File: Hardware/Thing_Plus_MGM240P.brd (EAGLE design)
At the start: 22.9 x 58.4 mm, 181 parts, among them J1 THING_PLUS_LOGICAL, J2 USB Female Type C Connector, J3 QWIIC_RIGHT_ANGLE, J5 MICRO-SDFRICTION, Q1 20V/4.2A/52mΩ/1.4W, U1 MGM240P, U2 XC6222B331MR-G, U3 EFM32GG12B410F1024GL120, U4 MCP73831, U5 MAX17048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

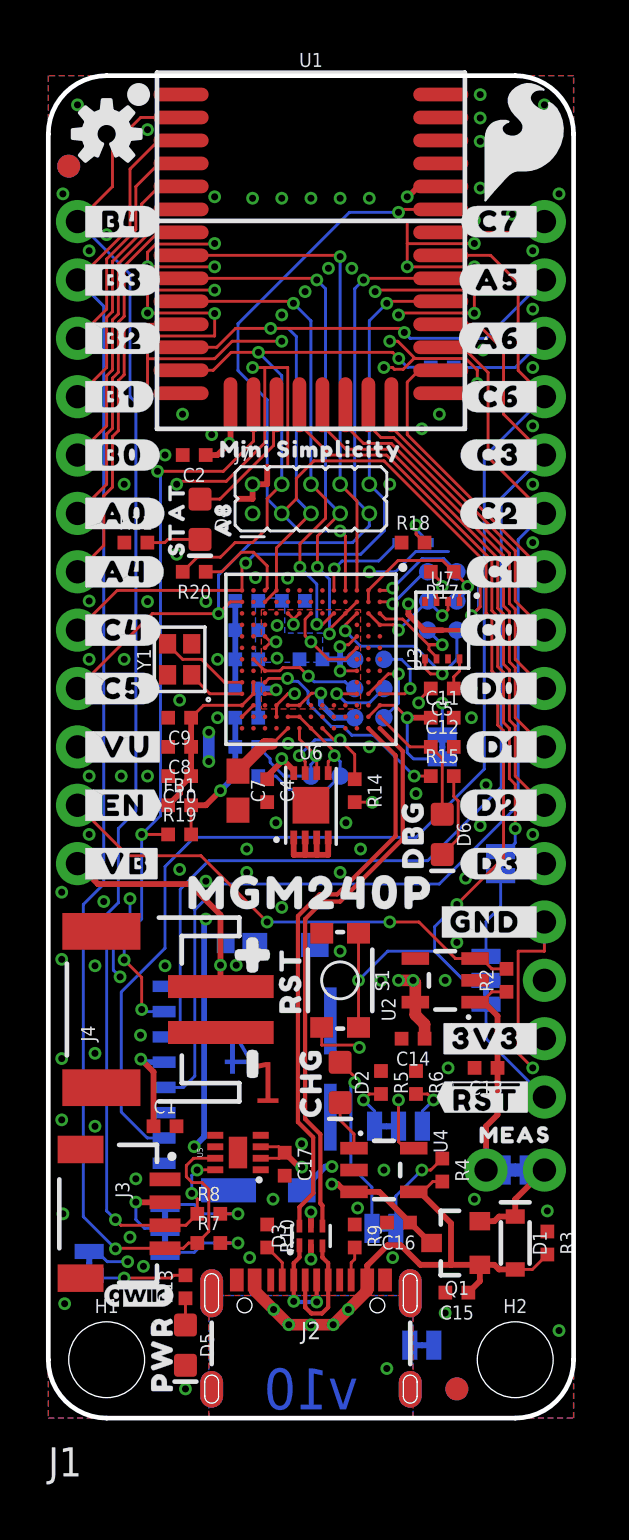
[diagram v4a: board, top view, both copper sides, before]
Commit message: Design review updates
Move RST jumper to align with D3_ISO jumper
Add silk label to CHG_I jumper
Move R20 left 25 mils
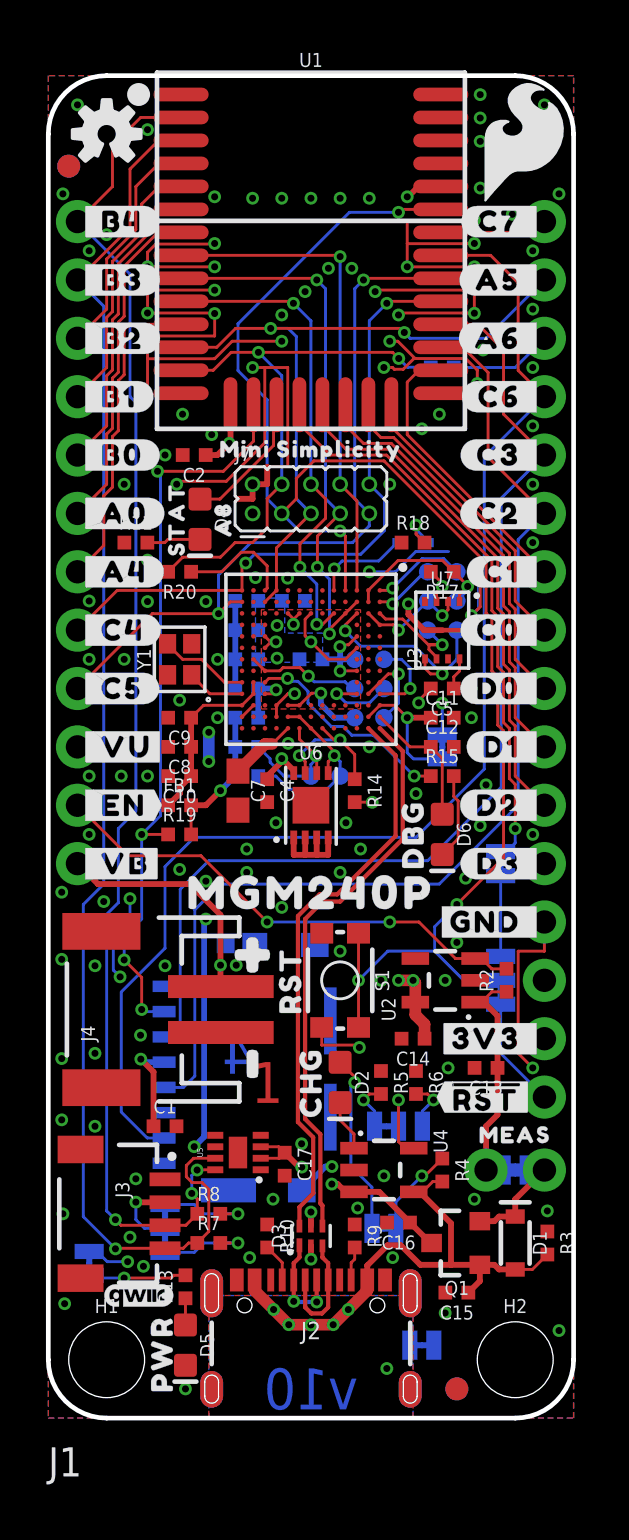
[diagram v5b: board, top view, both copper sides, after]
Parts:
- added U$83: (no value), output:#CHG_I#0
- moved U$80 0.64 mm to (19.1, 18.2)
- moved U$81 0.64 mm to (19.1, 19.9)
- moved R20 0.63 mm to (5.71, 36.8)
- moved RST 0.63 mm to (19.7, 19.1)
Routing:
- net RX/PA06: track 24.3 -> 24.9 mm
- net !RESET!: track 66.8 -> 67.5 mm
- net N$25: track 4.38 -> 5.01 mm
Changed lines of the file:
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@@
 <attribute name="VALUE" x="5.715" y="24.838" size="0.6096" layer="27" font="vector" ratio="20" align="top-center"/>
 </element>
-<element name="R20" library="SparkFun-Resistors" package="0402-TIGHT" value="330" x="6.35" y="36.83" smashed="yes" rot="R180">
-<attribute name="NAME" x="6.35" y="36.268" size="0.6096" layer="25" font="vector" ratio="20" rot="R180" align="bottom-center"/>
-<attribute name="PROD_ID" value="RES-15407" x="6.35" y="36.83" size="1.778" layer="27" rot="R180" display="off"/>
-<attribute name="VALUE" x="6.35" y="37.392" size="0.6096" layer="27" font="vector" ratio="20" rot="R180" align="top-center"/>
+<element name="R20" library="SparkFun-Resistors" package="0402-TIGHT" value="330" x="5.715" y="36.83" smashed="yes" rot="R180">
+<attribute name="NAME" x="5.715" y="36.268" size="0.6096" layer="25" font="vector" ratio="20" rot="R180" align="bottom-center"/>
+<attribute name="PROD_ID" value="RES-15407" x="5.715" y="36.83" size="1.778" layer="27" rot="R180" display="off"/>
+<attribute name="VALUE" x="5.715" y="37.392" size="0.6096" layer="27" font="vector" ratio="20" rot="R180" align="top-center"/>
 </element>
 <element name="R21" library="SparkFun-Resistors" package="0402-TIGHT" value="330" x="17.145" y="45.72" smashed="yes" rot="MR0">
@@
 </element>
 <element name="U$65" library="SEGGER-LOGO" package="SEGGER_LOGO" value="" x="9.269" y="44.45" smashed="yes" rot="MR0"/>
-<element name="RST" library="SparkFun-Jumpers" package="SMT-JUMPER_3_1-NC_TRACE_SILK" package3d_urn="urn:adsk.eagle:package:39288/1" value="JUMPER-SMT_3_1-NC_TRACE_SILK" x="19.05" y="19.05" smashed="yes" rot="MR270">
-<attribute name="NAME" x="17.907" y="19.05" size="0.6096" layer="26" font="vector" ratio="20" rot="MR270" align="bottom-center"/>
-<attribute name="VALUE" x="20.193" y="19.05" size="0.6096" layer="28" font="vector" ratio="20" rot="MR270" align="top-center"/>
+<element name="RST" library="SparkFun-Jumpers" package="SMT-JUMPER_3_1-NC_TRACE_SILK" package3d_urn="urn:adsk.eagle:package:39288/1" value="JUMPER-SMT_3_1-NC_TRACE_SILK" x="19.685" y="19.05" smashed="yes" rot="MR270">
+<attribute name="NAME" x="18.542" y="19.05" size="0.6096" layer="26" font="vector" ratio="20" rot="MR270" align="bottom-center"/>
+<attribute name="VALUE" x="20.828" y="19.05" size="0.6096" layer="28" font="vector" ratio="20" rot="MR270" align="top-center"/>
 </element>
 <element name="D3_ISO" library="SparkFun-Jumpers" package="SMT-JUMPER_2_NC_TRACE_SILK" package3d_urn="urn:adsk.eagle:package:39281/1" value="JUMPER-SMT_2_NC_TRACE_SILK" x="19.685" y="24.13" smashed="yes" rot="MR270">
@@
 <attribute name="VALUE" x="20.828" y="24.13" size="0.6096" layer="28" font="vector" ratio="20" rot="MR270" align="top-center"/>
 </element>
-<element name="U$80" library="output" package="#RST#0" value="" x="18.415" y="18.161" smashed="yes" rot="MR0"/>
-<element name="U$81" library="output" package="#D3#0" value="" x="18.415" y="19.939" smashed="yes" rot="MR0"/>
+<element name="U$80" library="output" package="#RST#0" value="" x="19.05" y="18.161" smashed="yes" rot="MR0"/>
+<element name="U$81" library="output" package="#D3#0" value="" x="19.05" y="19.939" smashed="yes" rot="MR0"/>
 <element name="U$82" library="output" package="#D3#4" value="" x="16.383" y="22.1615" smashed="yes" rot="MR0"/>
 <element name="U$47" library="SILICON-LABS-LOGO" package="SILICON_LABS_LOGO" value="" x="6.096" y="56.007" smashed="yes" rot="MR0"/>
+<element name="U$83" library="output" package="#CHG_I#0" value="" x="15.24" y="11.176" smashed="yes" rot="MR0"/>
 </elements>
 <signals>
@@
 <via x="17.272" y="19.05" extent="1-16" drill="0.3048"/>
 <via x="17.399" y="15.24" extent="1-16" drill="0.3048"/>
-<via x="14.605" y="10.795" extent="1-16" drill="0.3048"/>
+<via x="14.605" y="10.541" extent="1-16" drill="0.3048"/>
 <wire x1="18.5337" y1="48.0905" x2="18.542" y2="48.0822" width="0.127" layer="1"/>
 <wire x1="18.5337" y1="48.0905" x2="15.3245" y2="48.0905" width="0.127" layer="1"/>
@@
 <wire x1="11.4308875" y1="7.4939125" x2="11.4308875" y2="6.9164" width="0.254" layer="1"/>
 <via x="11.4308875" y="6.9164" extent="1-16" drill="0.3048"/>
-<via x="5.588" y="37.592" extent="1-16" drill="0.3048"/>
+<via x="4.318" y="37.338" extent="1-16" drill="0.3048"/>
 <via x="19.05" y="27.559" extent="1-16" drill="0.3048"/>
 <via x="18.796" y="25.781" extent="1-16" drill="0.3048"/>
@@
 <contactref element="R4" pad="1"/>
 <contactref element="CHG" pad="1"/>
-<via x="16.256" y="10.795" extent="1-16" drill="0.3048"/>
-<wire x1="16.256" y1="10.795" x2="16.645" y2="10.795" width="0.127" layer="1"/>
-<wire x1="16.645" y1="10.795" x2="17.145" y2="11.295" width="0.127" layer="1"/>
-<wire x1="15.1257" y1="8.255" x2="15.1257" y2="9.6647" width="0.127" layer="16"/>
-<wire x1="15.1257" y1="9.6647" x2="16.256" y2="10.795" width="0.127" layer="16"/>
+<via x="16.256" y="10.541" extent="1-16" drill="0.3048"/>
+<wire x1="16.256" y1="10.541" x2="16.391" y2="10.541" width="0.127" layer="1"/>
+<wire x1="16.391" y1="10.541" x2="17.145" y2="11.295" width="0.127" layer="1"/>
+<wire x1="15.1257" y1="8.255" x2="15.1257" y2="9.4107" width="0.127" layer="16"/>
+<wire x1="15.1257" y1="9.4107" x2="16.256" y2="10.541" width="0.127" layer="16"/>
 </signal>
 <signal name="N$14">
@@
 <wire x1="9.525" y1="40.005" x2="10.16" y2="40.64" width="0.127" layer="1"/>
 <contactref element="R20" pad="2"/>
-<wire x1="5.85" y1="36.83" x2="6.485" y2="37.465" width="0.127" layer="1"/>
+<wire x1="5.215" y1="36.83" x2="5.85" y2="37.465" width="0.127" layer="1"/>
 <wire x1="7.493" y1="37.465" x2="8.128" y2="38.1" width="0.127" layer="1"/>
-<wire x1="6.485" y1="37.465" x2="7.493" y2="37.465" width="0.127" layer="1"/>
+<wire x1="5.85" y1="37.465" x2="7.493" y2="37.465" width="0.127" layer="1"/>
 <wire x1="8.128" y1="38.1" x2="8.89" y2="38.1" width="0.127" layer="1"/>
 <wire x1="8.89" y1="38.1" x2="9.525" y2="38.735" width="0.127" layer="1"/>
@@
 <via x="13.5" y="19.05" extent="1-16" drill="0.3048"/>
 <wire x1="13.5" y1="19.05" x2="14.77" y2="20.32" width="0.127" layer="16"/>
-<wire x1="18.0815" y1="19.05" x2="19.05" y2="19.05" width="0.127" layer="16"/>
+<wire x1="18.0815" y1="19.05" x2="19.685" y2="19.05" width="0.127" layer="16"/>
 <wire x1="16.8115" y1="20.32" x2="18.0815" y2="19.05" width="0.127" layer="16"/>
 <wire x1="14.77" y1="20.32" x2="16.8115" y2="20.32" width="0.127" layer="16"/>
@@
 <wire x1="9.525" y1="37.084" x2="8.9281" y2="37.6809" width="0.127" layer="1"/>
 <wire x1="8.39645625" y1="37.6809" x2="8.9281" y2="37.6809" width="0.127" layer="1"/>
-<wire x1="6.85" y1="36.83" x2="7.54555625" y2="36.83" width="0.127" layer="1"/>
+<wire x1="6.215" y1="36.83" x2="7.54555625" y2="36.83" width="0.127" layer="1"/>
 <wire x1="7.54555625" y1="36.83" x2="8.39645625" y2="37.6809" width="0.127" layer="1"/>
 </signal>
@@
 <contactref element="RST" pad="3"/>
 <contactref element="J1" pad="28"/>
-<wire x1="21.59" y1="13.97" x2="19.05" y2="16.51" width="0.127" layer="16"/>
-<wire x1="19.05" y1="16.51" x2="19.05" y2="18.0086" width="0.127" layer="16"/>
+<wire x1="21.59" y1="13.97" x2="19.685" y2="15.875" width="0.127" layer="16"/>
+<wire x1="19.685" y1="15.875" x2="19.685" y2="18.0086" width="0.127" layer="16"/>
 </signal>
 <signal name="A0">
@@
 <contactref element="D3_ISO" pad="2"/>
 <contactref element="J1" pad="24"/>
-<wire x1="19.685" y1="23.6093" x2="19.685" y2="22.2504" width="0.127" layer="16"/>
-<wire x1="19.685" y1="22.2504" x2="19.05" y2="21.6154" width="0.127" layer="16"/>
-<wire x1="19.05" y1="21.6154" x2="19.05" y2="20.0914" width="0.127" layer="16"/>
+<wire x1="19.685" y1="23.6093" x2="19.685" y2="20.0914" width="0.127" layer="16"/>
 <wire x1="19.685" y1="23.6093" x2="21.0693" y2="23.6093" width="0.127" layer="16"/>
 <wire x1="21.0693" y1="23.6093" x2="21.59" y2="24.13" width="0.127" layer="16"/>

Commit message: Design review updates
Nudge RX/PA06 away from N$25
Add text to schematic explaining escape routing connections
Change RST jumper to "JP1" to make people read the docs
Remove "Thing Plus" from bottom silkscreen
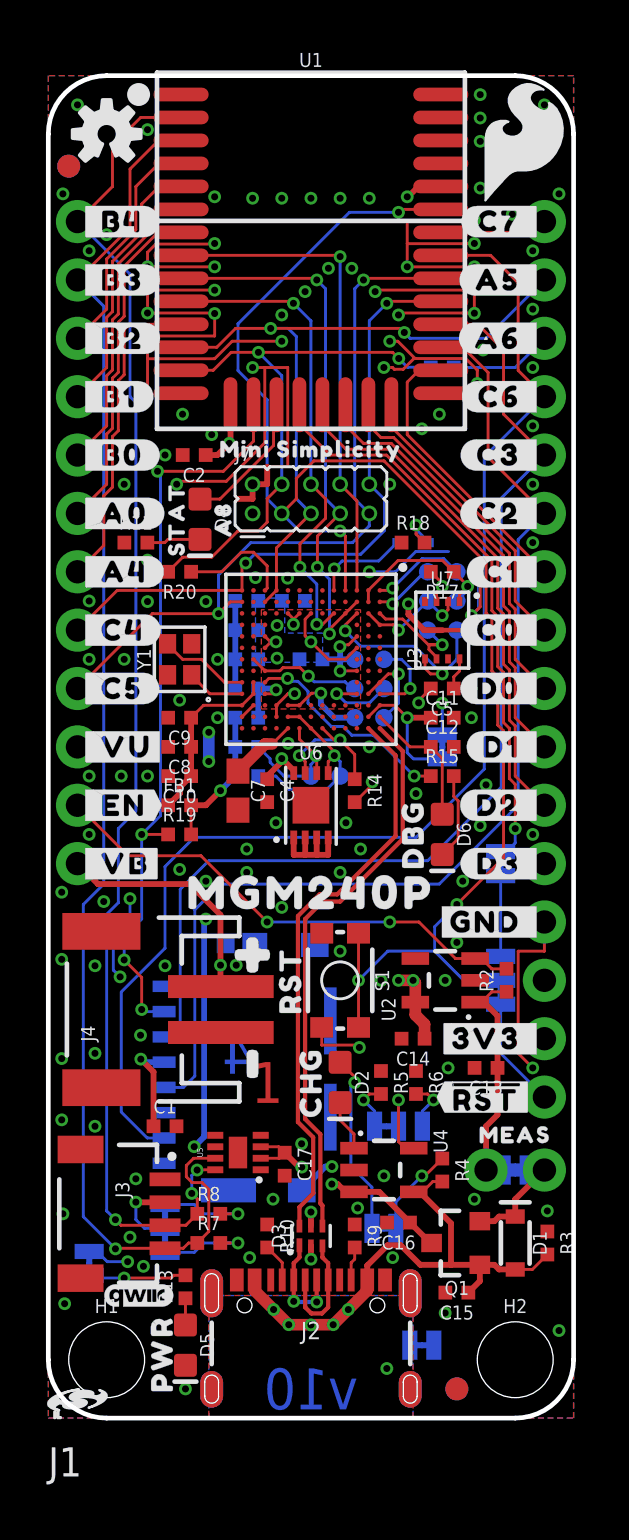
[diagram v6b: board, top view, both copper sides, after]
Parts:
- removed U$80: (no value), output:#RST#0
- removed U$81: (no value), output:#D3#0
- U$69: device output:THING_PLUS0 -> output:#JP1#0
- moved U$69 10.6 mm to (19.1, 18.2)
- moved U$82 3.21 mm to (18.9, 24.1)
- moved U$58 2.74 mm to (11.4, 26.7)
- renumbered RST to JP1

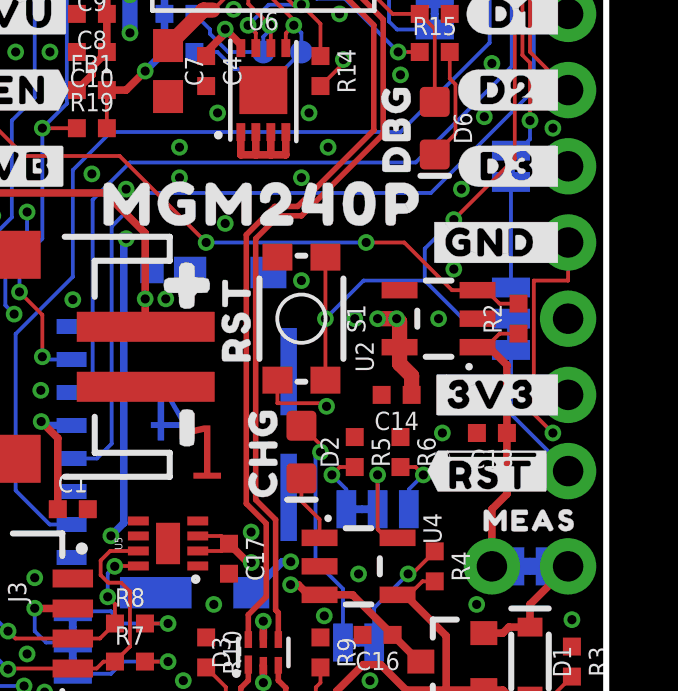
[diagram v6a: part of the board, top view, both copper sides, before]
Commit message: Design review changes
Fix acid traps
Change JP1 silk
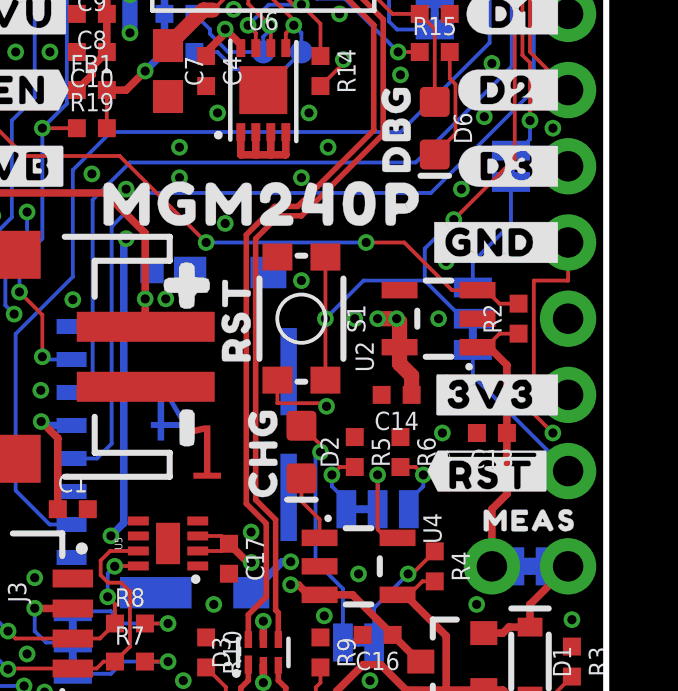
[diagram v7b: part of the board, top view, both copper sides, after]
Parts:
- added U$80: (no value), output:A0
- added U$81: (no value), output:B0
- moved JP1 1.27 mm to (18.4, 19.1)
- moved U$69 1.26 mm to (19.9, 19.1), turned to 90 degrees
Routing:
- net !RESET!: track 67.5 -> 66.2 mm
- net N$28: track 4.83 -> 5.35 mm
- net A0: track 5.64 -> 6.16 mm
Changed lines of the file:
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@@
 <vertex x="0.408365625" y="0.00025625"/>
 </polygon>
-<wire x1="15.875" y1="24.13" x2="15.24" y2="24.13" width="0.1524" layer="22"/>
-<wire x1="15.367" y1="19.558" x2="18.669" y2="19.558" width="0.1524" layer="22"/>
-<wire x1="15.24" y1="24.13" x2="14.605" y2="23.495" width="0.1524" layer="22"/>
-<wire x1="14.605" y1="23.495" x2="14.605" y2="20.32" width="0.1524" layer="22"/>
-<wire x1="14.605" y1="20.32" x2="15.367" y2="19.558" width="0.1524" layer="22"/>
 </plain>
 <attributes>
@@
 </element>
 <element name="U$65" library="SEGGER-LOGO" package="SEGGER_LOGO" value="" x="9.269" y="44.45" smashed="yes" rot="MR0"/>
-<element name="JP1" library="SparkFun-Jumpers" package="SMT-JUMPER_3_1-NC_TRACE_SILK" package3d_urn="urn:adsk.eagle:package:39288/1" value="JUMPER-SMT_3_1-NC_TRACE_SILK" x="19.685" y="19.05" smashed="yes" rot="MR270">
-<attribute name="NAME" x="18.542" y="19.05" size="0.6096" layer="26" font="vector" ratio="20" rot="MR270" align="bottom-center"/>
-<attribute name="VALUE" x="20.828" y="19.05" size="0.6096" layer="28" font="vector" ratio="20" rot="MR270" align="top-center"/>
+<element name="JP1" library="SparkFun-Jumpers" package="SMT-JUMPER_3_1-NC_TRACE_SILK" package3d_urn="urn:adsk.eagle:package:39288/1" value="JUMPER-SMT_3_1-NC_TRACE_SILK" x="18.415" y="19.05" smashed="yes" rot="MR270">
+<attribute name="NAME" x="17.272" y="19.05" size="0.6096" layer="26" font="vector" ratio="20" rot="MR270" align="bottom-center"/>
+<attribute name="VALUE" x="19.558" y="19.05" size="0.6096" layer="28" font="vector" ratio="20" rot="MR270" align="top-center"/>
 </element>
 <element name="D3_ISO" library="SparkFun-Jumpers" package="SMT-JUMPER_2_NC_TRACE_SILK" package3d_urn="urn:adsk.eagle:package:39281/1" value="JUMPER-SMT_2_NC_TRACE_SILK" x="19.685" y="24.13" smashed="yes" rot="MR270">
@@
 <element name="U$47" library="SILICON-LABS-LOGO" package="SILICON_LABS_LOGO" value="" x="6.096" y="56.007" smashed="yes" rot="MR0"/>
 <element name="U$83" library="output" package="#CHG_I#0" value="" x="15.24" y="11.176" smashed="yes" rot="MR0"/>
-<element name="U$69" library="output" package="#JP1#0" value="" x="19.05" y="18.161" smashed="yes" rot="MR0"/>
+<element name="U$69" library="output" package="#JP1#0" value="" x="19.939" y="19.05" smashed="yes" rot="MR90"/>
+<element name="U$80" library="output" package="A0" value="" x="16.764" y="18.161" smashed="yes" rot="MR90"/>
+<element name="U$81" library="output" package="B0" value="" x="16.764" y="20.066" smashed="yes" rot="MR90"/>
 </elements>
 <signals>
@@
 <via x="21.082" y="25.4" extent="1-16" drill="0.3048"/>
 <via x="0.635" y="8.89" extent="1-16" drill="0.3048"/>
-<via x="17.78" y="20.701" extent="1-16" drill="0.3048"/>
+<via x="17.526" y="20.955" extent="1-16" drill="0.3048"/>
 <via x="18.034" y="23.368" extent="1-16" drill="0.3048"/>
 <via x="14.478" y="19.05" extent="1-16" drill="0.3048"/>
@@
 <contactref element="R6" pad="2"/>
 <contactref element="CHG_I" pad="1"/>
-<wire x1="16.764" y1="13.843" x2="16.2814" y2="13.3604" width="0.127" layer="16"/>
-<wire x1="16.2814" y1="13.3604" x2="16.2814" y2="12.7" width="0.127" layer="16"/>
+<wire x1="16.764" y1="13.843" x2="16.764" y2="13.462" width="0.127" layer="16"/>
+<wire x1="16.764" y1="13.462" x2="16.2814" y2="12.9794" width="0.127" layer="16"/>
+<wire x1="16.2814" y1="12.9794" x2="16.2814" y2="12.7" width="0.127" layer="16"/>
 <via x="16.764" y="13.843" extent="1-16" drill="0.3048"/>
 <wire x1="16.002" y1="14.105" x2="16.502" y2="14.105" width="0.127" layer="1"/>
@@
 <contactref element="R5" pad="2"/>
 <contactref element="CHG_I" pad="3"/>
-<wire x1="13.716" y1="13.843" x2="14.1986" y2="13.3604" width="0.127" layer="16"/>
-<wire x1="14.1986" y1="13.3604" x2="14.1986" y2="12.7" width="0.127" layer="16"/>
+<wire x1="14.1986" y1="12.9794" x2="13.716" y2="13.462" width="0.127" layer="16"/>
+<wire x1="13.716" y1="13.843" x2="13.716" y2="13.462" width="0.127" layer="16"/>
+<wire x1="14.1986" y1="12.9794" x2="14.1986" y2="12.7" width="0.127" layer="16"/>
 <via x="13.716" y="13.843" extent="1-16" drill="0.3048"/>
 <wire x1="14.478" y1="14.105" x2="13.978" y2="14.105" width="0.127" layer="1"/>
@@
 <via x="13.5" y="19.05" extent="1-16" drill="0.3048"/>
 <wire x1="13.5" y1="19.05" x2="14.77" y2="20.32" width="0.127" layer="16"/>
-<wire x1="18.0815" y1="19.05" x2="19.685" y2="19.05" width="0.127" layer="16"/>
+<wire x1="18.0815" y1="19.05" x2="18.415" y2="19.05" width="0.127" layer="16"/>
 <wire x1="16.8115" y1="20.32" x2="18.0815" y2="19.05" width="0.127" layer="16"/>
 <wire x1="14.77" y1="20.32" x2="16.8115" y2="20.32" width="0.127" layer="16"/>
@@
 <contactref element="JP1" pad="3"/>
 <contactref element="J1" pad="28"/>
-<wire x1="21.59" y1="13.97" x2="19.685" y2="15.875" width="0.127" layer="16"/>
-<wire x1="19.685" y1="15.875" x2="19.685" y2="18.0086" width="0.127" layer="16"/>
+<wire x1="21.59" y1="13.97" x2="18.415" y2="17.145" width="0.127" layer="16"/>
+<wire x1="18.415" y1="17.145" x2="18.415" y2="18.0086" width="0.127" layer="16"/>
 </signal>
 <signal name="A0">
@@
 <contactref element="D3_ISO" pad="2"/>
 <contactref element="J1" pad="24"/>
-<wire x1="19.685" y1="23.6093" x2="19.685" y2="20.0914" width="0.127" layer="16"/>
+<wire x1="19.685" y1="23.6093" x2="19.685" y2="22.2123" width="0.127" layer="16"/>
+<wire x1="19.685" y1="22.2123" x2="18.415" y2="20.9423" width="0.127" layer="16"/>
+<wire x1="18.415" y1="20.9423" x2="18.415" y2="20.0914" width="0.127" layer="16"/>
 <wire x1="19.685" y1="23.6093" x2="21.0693" y2="23.6093" width="0.127" layer="16"/>
 <wire x1="21.0693" y1="23.6093" x2="21.59" y2="24.13" width="0.127" layer="16"/>
